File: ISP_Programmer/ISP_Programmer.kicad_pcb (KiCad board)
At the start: 2 copper layers, 35 x 29 mm, 19 parts, among them IC1 ATTINY2313-S, P1 CONN_02X03, P2 USB_OTG, P3 CONN_02X03, U2 74LS125, X1 CRYSTAL_SMD

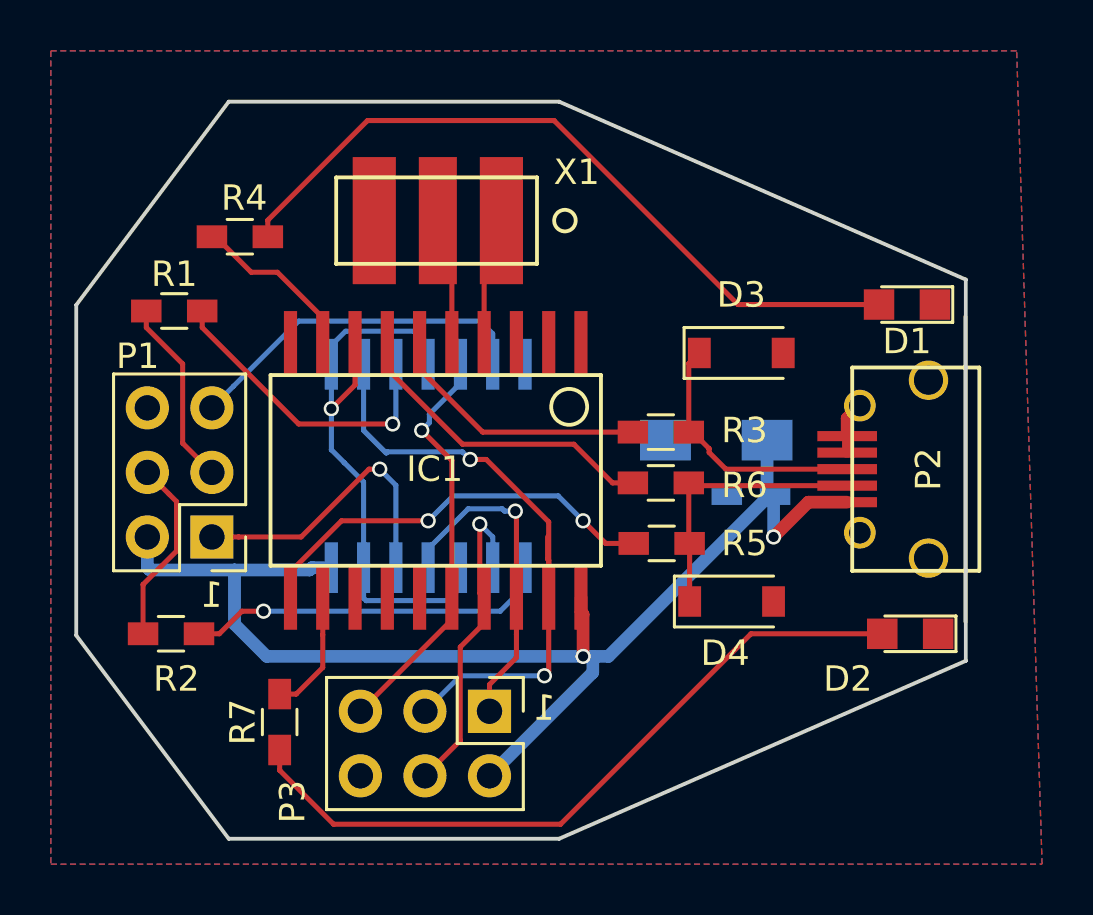
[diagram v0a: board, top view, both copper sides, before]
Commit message: added ISP programmer reset pull up
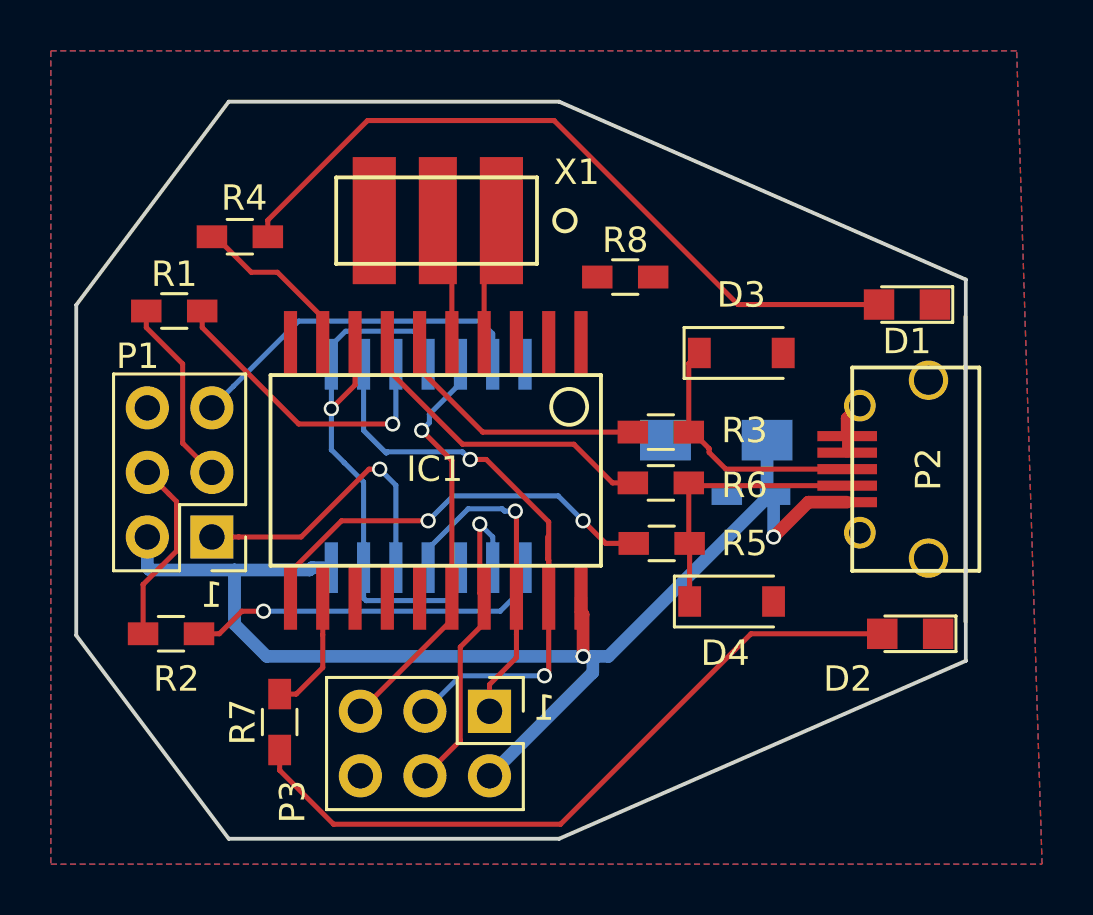
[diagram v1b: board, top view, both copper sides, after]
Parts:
- added R8: 10K, Resistors_SMD:R_0603_HandSoldering, F.Cu at (172.6, 108.9)
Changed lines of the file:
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@@
 (kicad_pcb (version 4) (host pcbnew 4.0.4-stable)
   (general
-    (links 54)
-    (no_connects 10)
+    (links 56)
+    (no_connects 2)
     (area 150.924999 101.924999 186.075001 131.075001)
     (thickness 1.6)
@@
     (tracks 191)
     (zones 0)
-    (modules 19)
+    (modules 20)
     (nets 31)
   )
@@
   )
   (setup
-    (last_trace_width 0.5)
+    (last_trace_width 0.2)
     (user_trace_width 0.5)
     (trace_clearance 0.2)
@@
     (pad_to_mask_clearance 0.2)
     (aux_axis_origin 0 0)
-    (visible_elements FFFFFF7F)
+    (visible_elements 7FFFFFFF)
     (pcbplotparams
       (layerselection 0x00030_80000001)
@@
       (net 2 GND))
   )
-  (gr_text 1 (at 156.337 121.412 360) (layer F.SilkS)
+  (module Resistors_SMD:R_0603_HandSoldering (layer F.Cu)
+    (at 172.6 108.9)
+    (descr "Resistor SMD 0603, hand soldering")
+    (tags "resistor 0603")
+    (attr smd)
+    (fp_text reference R8 (at 0 -1.45) (layer F.SilkS)
+      (effects (font (size 1 1) (thickness 0.15)))
+    )
+    (fp_text value 10K (at 0 1.55) (layer F.Fab)
+      (effects (font (size 1 1) (thickness 0.15)))
+    )
+    (fp_text user %R (at 0 0) (layer F.Fab)
+      (effects (font (size 0.5 0.5) (thickness 0.075)))
+    )
+    (fp_line (start -0.8 0.4) (end -0.8 -0.4) (layer F.Fab) (width 0.1))
+    (fp_line (start 0.8 0.4) (end -0.8 0.4) (layer F.Fab) (width 0.1))
+    (fp_line (start 0.8 -0.4) (end 0.8 0.4) (layer F.Fab) (width 0.1))
+    (fp_line (start -0.8 -0.4) (end 0.8 -0.4) (layer F.Fab) (width 0.1))
+    (fp_line (start 0.5 0.68) (end -0.5 0.68) (layer F.SilkS) (width 0.12))
+    (fp_line (start -0.5 -0.68) (end 0.5 -0.68) (layer F.SilkS) (width 0.12))
+    (fp_line (start -1.96 -0.7) (end 1.95 -0.7) (layer F.CrtYd) (width 0.05))
+    (fp_line (start -1.96 -0.7) (end -1.96 0.7) (layer F.CrtYd) (width 0.05))
+    (fp_line (start 1.95 0.7) (end 1.95 -0.7) (layer F.CrtYd) (width 0.05))
+    (fp_line (start 1.95 0.7) (end -1.96 0.7) (layer F.CrtYd) (width 0.05))
+    (pad 1 smd rect (at -1.1 0) (size 1.2 0.9) (layers F.Cu F.Paste F.Mask)
+      (net 23 "Net-(IC1-Pad1)"))
+    (pad 2 smd rect (at 1.1 0) (size 1.2 0.9) (layers F.Cu F.Paste F.Mask)
+      (net 1 VCC))
+    (model ${KISYS3DMOD}/Resistors_SMD.3dshapes/R_0603.wrl
+      (at (xyz 0 0 0))
+      (scale (xyz 1 1 1))
+      (rotate (xyz 0 0 0))
+    )
+  )
+  (gr_text 1 (at 156.337 121.412) (layer F.SilkS)
     (effects (font (size 1 1) (thickness 0.15)) (justify mirror))
   )
